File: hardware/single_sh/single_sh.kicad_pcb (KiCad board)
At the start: 4 copper layers, 122 x 20 mm, 151 parts, among them J1 USB-C, J11 M1+M2, J12 M3+M4, J13 M5+M6, J14 M7+M8, J15 M9+M10, J2 Qwiic, J3 Qwiic, J4 5V IN, J5 LED STRIP, J6 LED PWR, J7 E-STOP, J8 PANEL BTN, Q1 AO3401A, SW1 BTN1, SW2 BTN2, SW3 BOOTSEL, U1 AT8833CQ, U10 AT8833CQ, U11 RP2354B, U12 TPD2E2U06, U13 ME6211C33M5G, U14 74AHCT1G125, U15 74AHCT1G125, U2 AT8833CQ, U3 AT8833CQ, U4 AT8833CQ, U5 AT8833CQ, U6 AT8833CQ, U7 AT8833CQ, U8 AT8833CQ, U9 AT8833CQ, Y1 12MHz

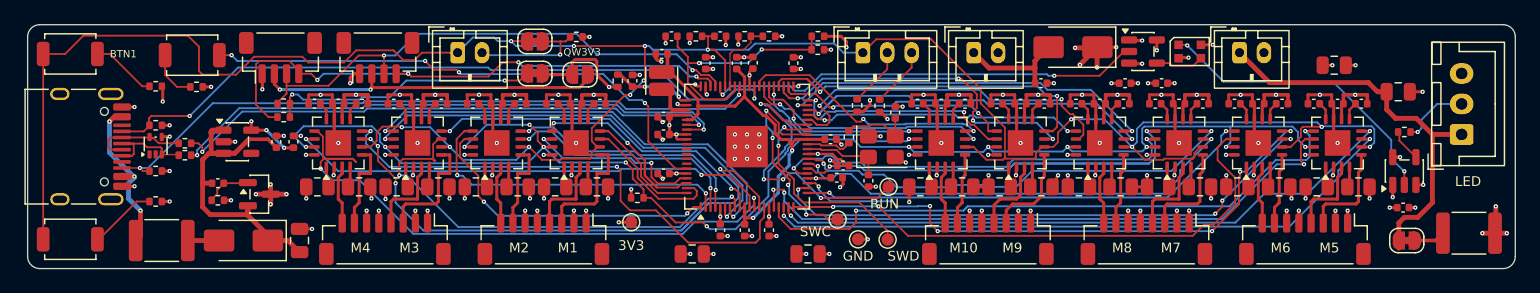
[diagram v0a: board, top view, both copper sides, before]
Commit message: single_sh: 0603 sense resistors; refilled zones, fab output
Sense resistors move from 0805 to 0603 (Viking SR731JTTDR820F, C186570,
250 mW); holding a coil at the current-limit trip is now 28 % of rating.
Swapped in place on the routed board: ISEN pad kept, GND pad 0.275 mm
inboard (R5/R11 keep the GND pad instead). Zones refilled after the route
cleanup and trace edits. DRC: 0 unconnected, 0 parity, no copper
violations; 4 silkscreen warnings.

Schematics, BOMs, generators and README updated; JLCPCB Gerbers/BOM/CPL
regenerated and placement-checked.

Co-Authored-By: Claude Opus 5.5 <noreply@anthropic.com>
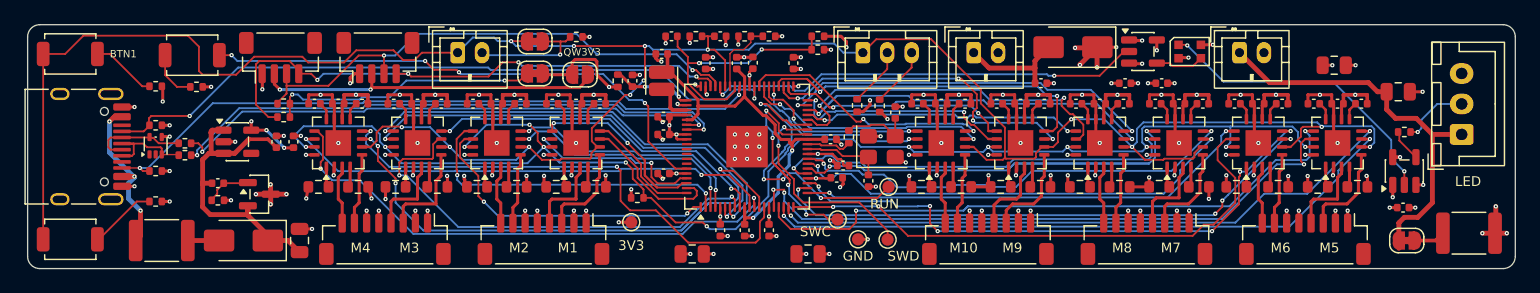
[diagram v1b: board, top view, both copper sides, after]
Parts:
- R1, R10, R11, R12, R13, R14, R15, R16, R17, R18, R19, R2, R20, R3, R4, R5, R6, R7, R8, R9: footprint Resistor_SMD:R_0805_2012Metric -> Resistor_SMD:R_0603_1608Metric
- moved R11 0.09 mm to (138.1, 103.3)
- moved R13 0.09 mm to (131.8, 103.3)
- moved R15 0.09 mm to (125.3, 103.3)
- moved R17 0.09 mm to (118.8, 103.3)
- moved R18 0.09 mm to (122.0, 103.3)
- moved R19 0.09 mm to (112.3, 103.3)
- moved R2 0.09 mm to (85.6, 103.3)
- moved R20 0.09 mm to (115.5, 103.3)
- moved R4 0.09 mm to (79.1, 103.3)
- moved R5 0.09 mm to (69.2, 103.3)
- moved R6 0.09 mm to (72.6, 103.3)
- moved R8 0.09 mm to (66.1, 103.3)
- moved R9 0.09 mm to (144.8, 103.3)
- moved R7 0.09 mm to (62.8, 103.3)
- moved R1 0.09 mm to (82.3, 103.3)
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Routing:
- net M4_AIN2: track 49.2 -> 43.7 mm
- net M1_BOUT1: track 9.89 -> 7.89 mm
- net M2_BOUT1: track 7.40 -> 5.86 mm
- net M4_BOUT1: track 7.40 -> 5.86 mm
- net M3_BOUT1: track 9.89 -> 8.35 mm
- net M3_BIN1: track 37.5 -> 37.0 mm

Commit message: single_sh_proto: all-0603 basic-parts prototype board, as ordered
150 x 30 mm 4-layer board, fully routed (0.52/0.3 vias, 45-degree traces,
centred pad entries, no vias in pads), JLCDFM clean. Corrected nested
dual-motor connector pinout, bring-up test points, back-silk squid art.
L1 substituted (C411344); status LED D2 is the 5050 WS2812B (C2843785),
left off the Economic PCBA order for hand soldering.

Generator updates for the proto board (build.py, pcbgen.py, jlcfab.py,
single_sh_sch.py, add_testpoints.py, squid_silk.py) and regenerated
outputs for the other boards.

Ordered from JLCPCB 2026-10-11: 5 boards, Economic PCBA.

Co-Authored-By: Claude Opus 5.5 <noreply@anthropic.com>
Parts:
- R1, R10, R11, R12, R13, R14, R15, R16, R17, R18, R19, R2, R20, R3, R4, R5, R6, R7, R8, R9: value 0.82 -> 1
